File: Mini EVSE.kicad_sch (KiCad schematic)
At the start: 33 parts, among them IC1 G3MC-201PL DC5, IC2 IRM-03-5, IC3 ATtiny84-20P, IC4 TMR1-0522, IC5 SI8261BAC-C-IP, J1 RE OUT, J10 M, J2 AC IN, J4 ICP, J5 SWITCH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

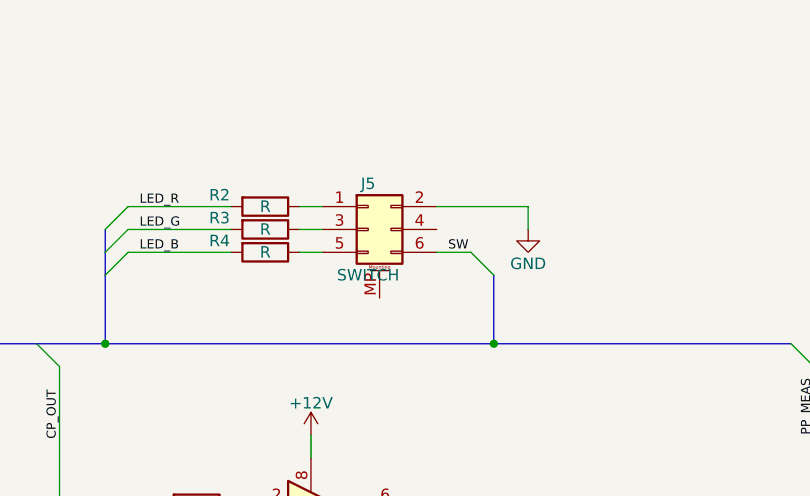
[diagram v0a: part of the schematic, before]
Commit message: Changed to correct switch connector
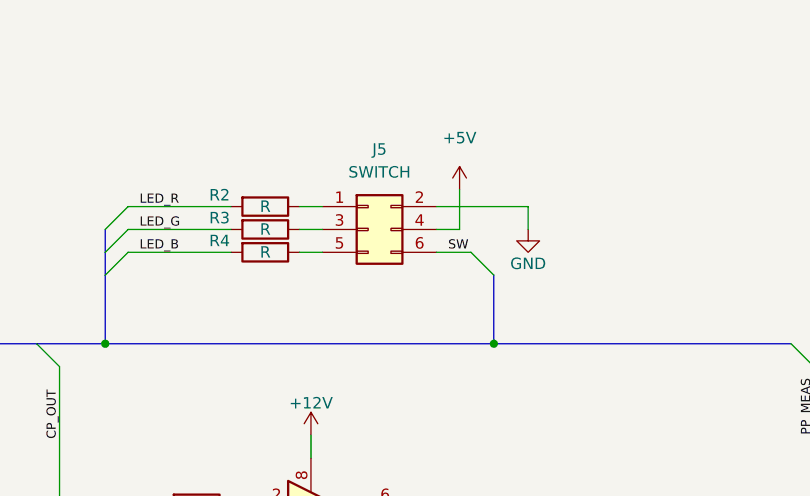
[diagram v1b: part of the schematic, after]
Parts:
- removed J5: SWITCH, Pin_Headers:Pin_Header_Straight_2x03_Pitch2.54mm, symbol Connector_Generic_MountingPin:Conn_02x03_Odd_Even_MountingPin
- added J5: SWITCH, symbol Connector_Generic:Conn_02x03_Odd_Even
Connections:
- net +5V: now also J5.4 (Pin_4)
- net GND: now also J5.2 (Pin_2)
- net SW: now also J5.6 (Pin_6)
- net at R2.1: now also J5.1 (Pin_1)
- net at R3.1: now also J5.3 (Pin_3)
- net at R4.1: now also J5.5 (Pin_5)
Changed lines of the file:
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@@
+    (stroke (width 0) (type default) (color 0 0 0 0))
+  )
+  (wire (pts (xy 176.53 44.45) (xy 179.07 44.45))
     (stroke (width 0) (type default) (color 0 0 0 0))
   )
@@
   )
   (wire (pts (xy 39.37 171.45) (xy 44.45 171.45))
+    (stroke (width 0) (type default) (color 0 0 0 0))
+  )
+  (wire (pts (xy 179.07 44.45) (xy 179.07 40.005))
     (stroke (width 0) (type default) (color 0 0 0 0))
   )
@@
     (pin "1")
     (pin "2")
-  )
-  (symbol (lib_id "Connector_Generic_MountingPin:Conn_02x03_Odd_Even_MountingPin") (at 168.91 44.45 0) (unit 1)
-    (in_bom yes) (on_board yes)
-    (property "Reference" "J5" (id 0) (at 168.91 39.37 0))
-    (property "Value" "SWITCH" (id 1) (at 168.91 49.53 0))
-    (property "Footprint" "Pin_Headers:Pin_Header_Straight_2x03_Pitch2.54mm" (id 2) (at 168.91 44.45 0)
-      (effects (font (size 1.27 1.27)) hide)
-    )
-    (property "Datasheet" "~" (id 3) (at 168.91 44.45 0)
-      (effects (font (size 1.27 1.27)) hide)
-    )
-    (pin "1")
-    (pin "2")
-    (pin "3")
-    (pin "4")
-    (pin "5")
-    (pin "6")
-    (pin "MP")
   )
   (symbol (lib_id "power:GND") (at 186.69 44.45 0) (unit 1)
@@
     (pin "9")
   )
+  (symbol (lib_id "Connector_Generic:Conn_02x03_Odd_Even") (at 168.91 44.45 0) (unit 1)
+    (in_bom yes) (on_board yes) (fields_autoplaced)
+    (property "Reference" "J5" (id 0) (at 170.18 35.56 0))
+    (property "Value" "SWITCH" (id 1) (at 170.18 38.1 0))
+    (property "Footprint" "" (id 2) (at 168.91 44.45 0)
+      (effects (font (size 1.27 1.27)) hide)
+    )
+    (property "Datasheet" "~" (id 3) (at 168.91 44.45 0)
+      (effects (font (size 1.27 1.27)) hide)
+    )
+    (pin "1")
+    (pin "2")
+    (pin "3")
+    (pin "4")
+    (pin "5")
+    (pin "6")
+  )
+  (symbol (lib_id "power:+5V") (at 179.07 40.005 0) (unit 1)
+    (in_bom yes) (on_board yes) (fields_autoplaced)
+    (property "Reference" "#PWR?" (id 0) (at 179.07 43.815 0)
+      (effects (font (size 1.27 1.27)) hide)
+    )
+    (property "Value" "+5V" (id 1) (at 179.07 34.29 0))
+    (property "Footprint" "" (id 2) (at 179.07 40.005 0)
+      (effects (font (size 1.27 1.27)) hide)
+    )
+    (property "Datasheet" "" (id 3) (at 179.07 40.005 0)
+      (effects (font (size 1.27 1.27)) hide)
+    )
+    (pin "1")
+  )
   (sheet_instances
     (path "/" (page "1"))
@@
       (reference "#PWR023") (unit 1) (value "GND") (footprint "")
     )
+    (path "/a3f3252a-453d-4c17-a856-332640621e05"
+      (reference "#PWR?") (unit 1) (value "+5V") (footprint "")
+    )
     (path "/00000000-0000-0000-0000-000059a14897"
       (reference "C1") (unit 1) (value "18p") (footprint "Miscellaneous:C_Disc_D2.5mm_W3.2mm_P2.54mm")
@@
       (reference "J4") (unit 1) (value "ICP") (footprint "Pin_Headers:Pin_Header_Straight_2x03_Pitch2.54mm")
     )
-    (path "/00000000-0000-0000-0000-000059a7109b"
-      (reference "J5") (unit 1) (value "SWITCH") (footprint "Pin_Headers:Pin_Header_Straight_2x03_Pitch2.54mm")
+    (path "/2236318d-525c-41c1-ab1c-1f70c3607037"
+      (reference "J5") (unit 1) (value "SWITCH") (footprint "")
     )
     (path "/00000000-0000-0000-0000-000059a7028d"

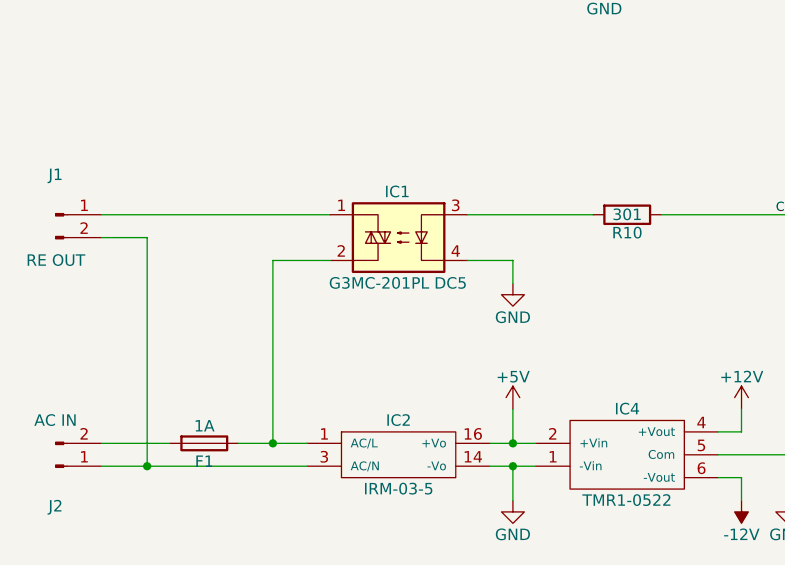
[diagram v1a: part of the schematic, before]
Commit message: Updated solid state relay
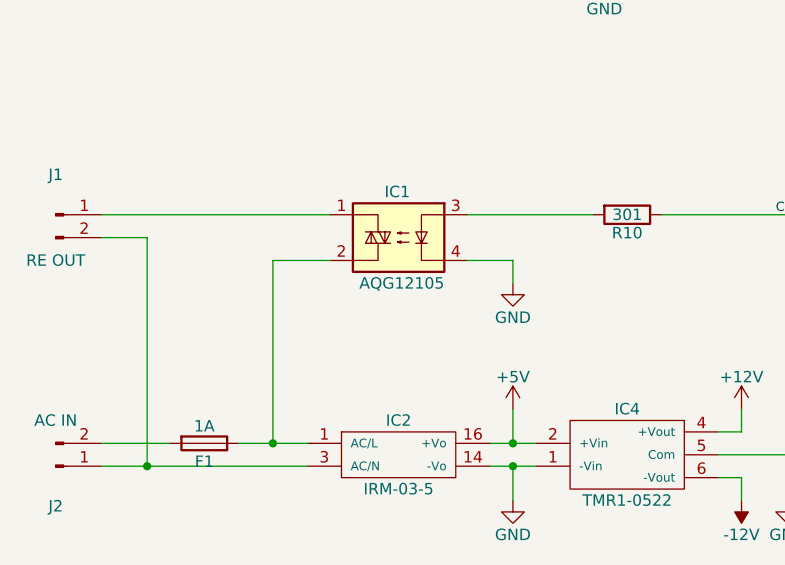
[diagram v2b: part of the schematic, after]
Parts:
- IC1: value G3MC-201PL DC5 -> AQG12105
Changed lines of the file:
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@@
       (effects (font (size 1.27 1.27)) (justify left))
     )
-    (property "Value" "G3MC-201PL DC5" (id 1) (at 80.01 151.13 0)
+    (property "Value" "AQG12105" (id 1) (at 77.47 151.13 0)
       (effects (font (size 1.27 1.27)) (justify left))
     )
@@
     )
     (path "/00000000-0000-0000-0000-000059a74096"
-      (reference "IC1") (unit 1) (value "G3MC-201PL DC5") (footprint "Package_SIP:SIP4_Sharp-SSR_P7.62mm_Straight")
+      (reference "IC1") (unit 1) (value "AQG12105") (footprint "Package_SIP:SIP4_Sharp-SSR_P7.62mm_Straight")
     )
     (path "/00000000-0000-0000-0000-000059a6ed36"
